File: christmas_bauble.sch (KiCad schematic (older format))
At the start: 49 parts, among them Q1 Q_NPN_EBC, Q2 Q_NPN_EBC, Q3 Q_NPN_EBC, Q4 Q_NPN_EBC, Q5 Q_NPN_EBC, SW1 SW_PUSH, SW2 SW_PUSH, SW3 SWITCH_INV, U1 595_SHIFT, U2 555

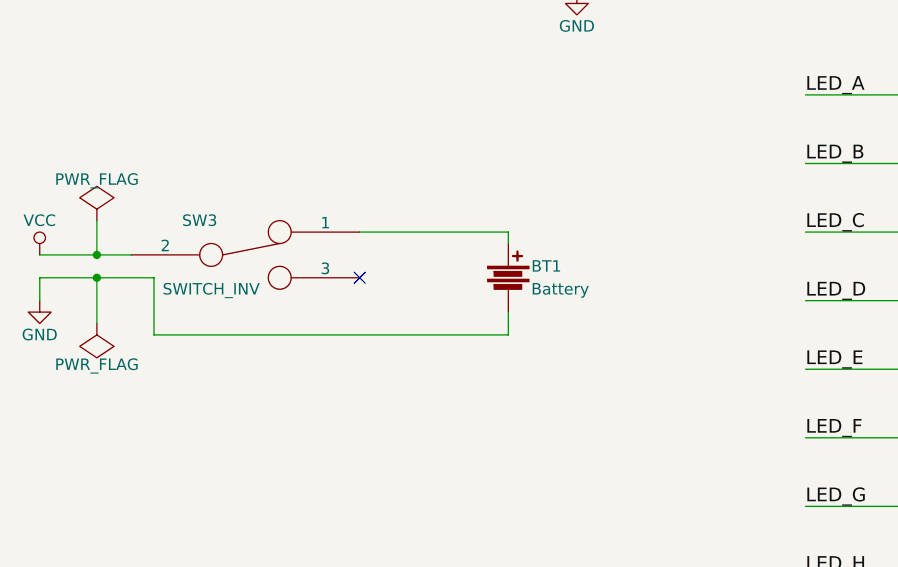
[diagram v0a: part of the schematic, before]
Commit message: Changing batteries on the board to 2 20mm coin cell batteries in paralell for longer lifetime. Routing batteries on the back via SMD holders.
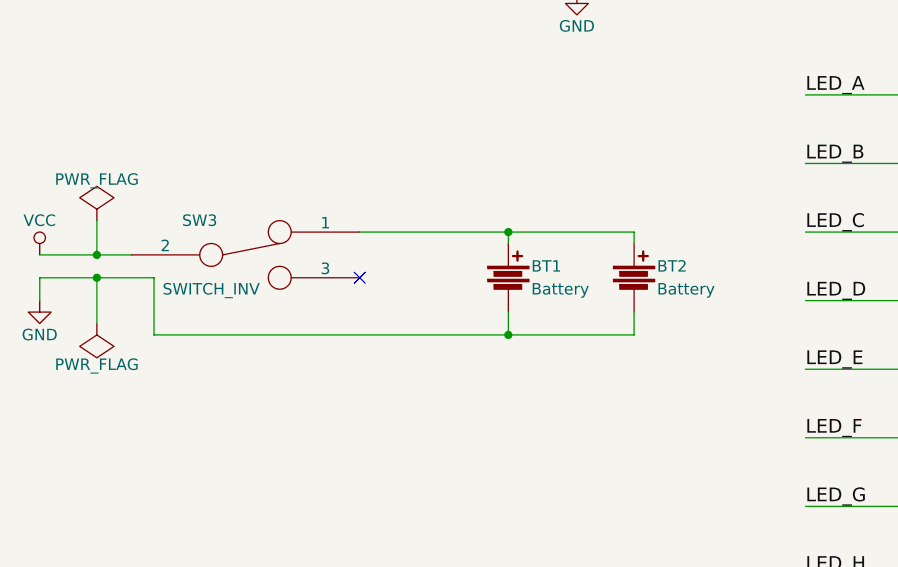
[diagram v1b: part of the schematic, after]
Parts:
- added BT2: Battery, kookie_utilities:20mm_coin_bat_smd, symbol Battery
- BT1: footprint kookie_utilities:COIN_BAT_HOLDER -> kookie_utilities:20mm_coin_bat_smd
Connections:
- net GND: now also BT2.2
- net at BT1.1, SW3.1: now also BT2.1
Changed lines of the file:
@@
 LIBS:contrib
 LIBS:valves
-LIBS:christmas_bauble
 LIBS:christmas_bauble-cache
 EELAYER 25 0
@@
 F 0 "BT1" H 3300 5900 50  0000 L CNN
 F 1 "Battery" H 3300 5800 50  0000 L CNN
-F 2 "kookie_utilities:COIN_BAT_HOLDER" V 3200 5890 60  0001 C CNN
+F 2 "kookie_utilities:20mm_coin_bat_smd" V 3200 5890 60  0001 C CNN
 F 3 "" V 3200 5890 60  0000 C CNN
 	1    3200 5850
@@
 	3200 5700 3200 5650
 Wire Wire Line
-	3200 5650 2550 5650
+	2550 5650 3750 5650
 Wire Wire Line
 	1650 5850 1650 6100
 Wire Wire Line
-	1650 6100 3200 6100
+	1650 6100 3750 6100
 Wire Wire Line
 	3200 6100 3200 6000
+$Comp
+L Battery BT2
+U 1 1 564B0785
+P 3750 5850
+F 0 "BT2" H 3850 5900 50  0000 L CNN
+F 1 "Battery" H 3850 5800 50  0000 L CNN
+F 2 "kookie_utilities:20mm_coin_bat_smd" V 3750 5890 60  0001 C CNN
+F 3 "" V 3750 5890 60  0000 C CNN
+	1    3750 5850
+	1    0    0    -1
+$EndComp
+Wire Wire Line
+	3750 5650 3750 5700
+Connection ~ 3200 5650
+Wire Wire Line
+	3750 6100 3750 6000
+Connection ~ 3200 6100
 $EndSCHEMATC
